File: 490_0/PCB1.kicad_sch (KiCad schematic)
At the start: 3 parts, among them J10 Conn_01x11, J3 Conn_01x08, J4 5051102291

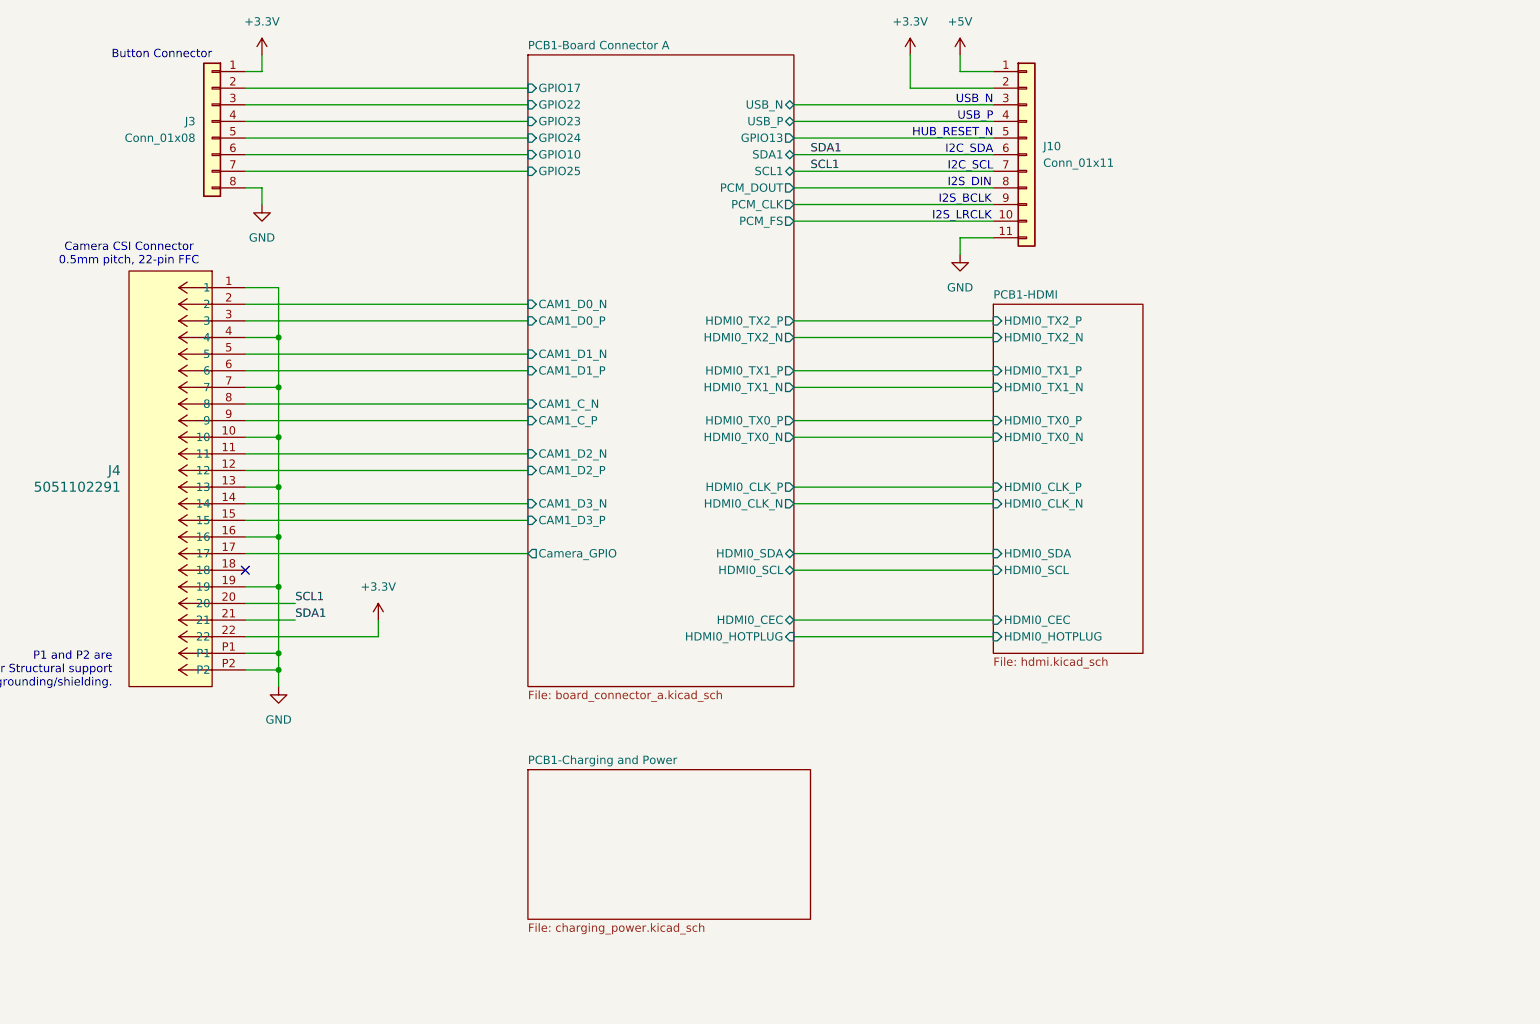
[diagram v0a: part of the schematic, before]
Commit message: Cleaned up global labels
TO DO: power chip change
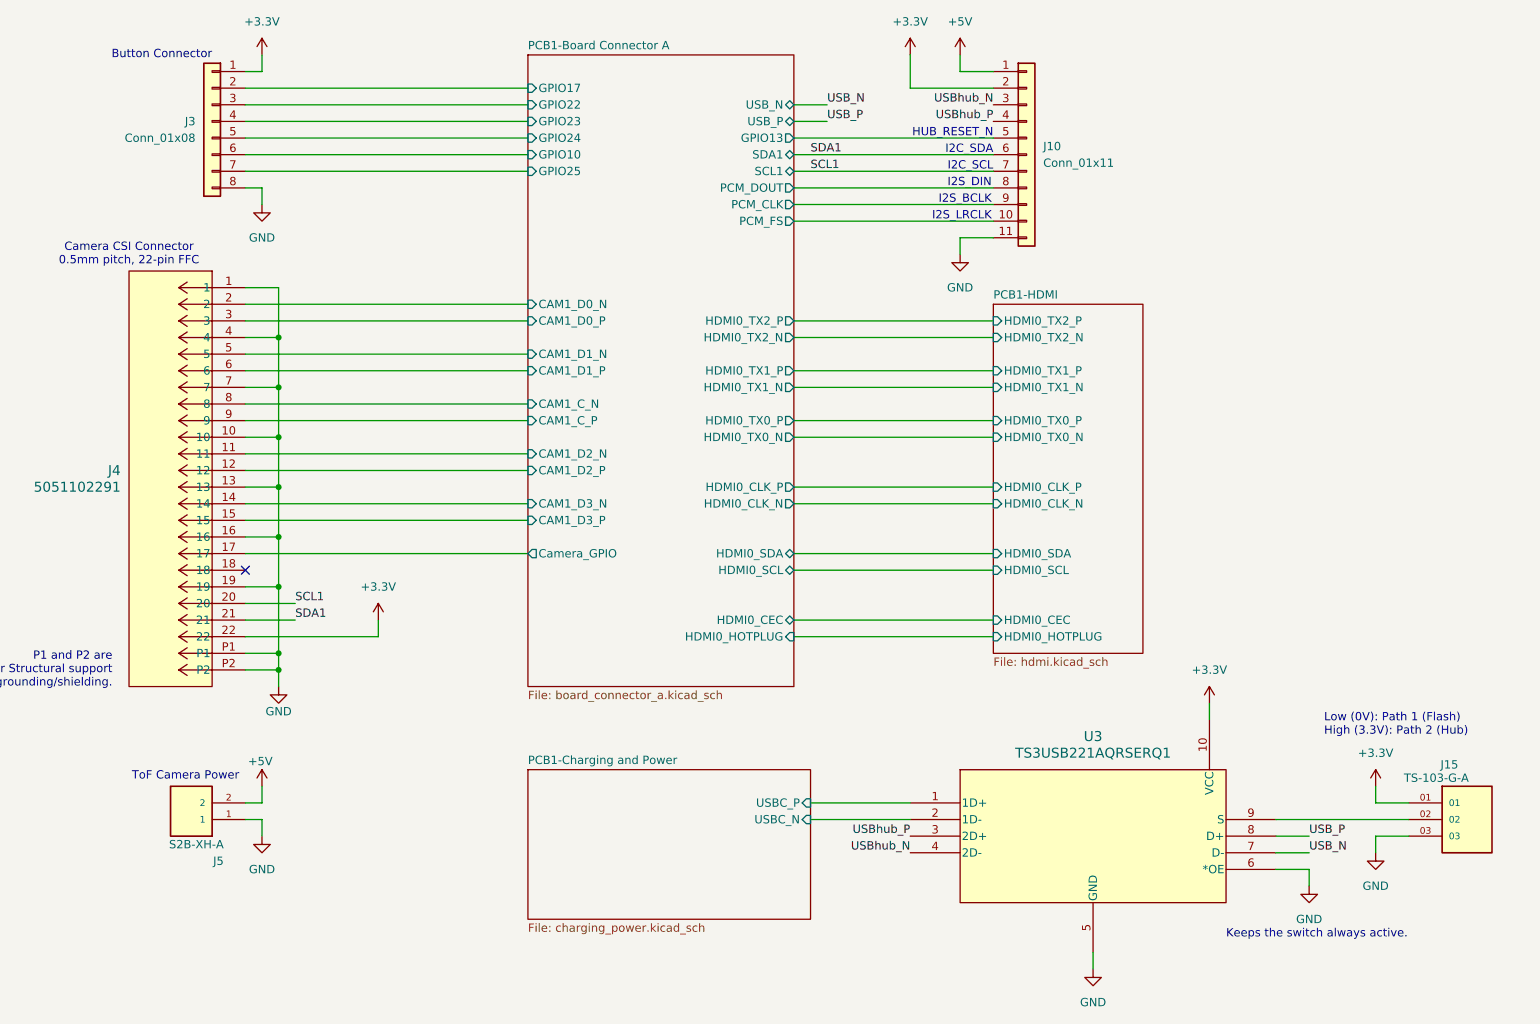
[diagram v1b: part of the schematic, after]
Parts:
- added J15: TS-103-G-A, TS-103-G-A:SAMTEC_TS-103-G-A, symbol capstone_parts:TS-103-G-A
- added J5: S2B-XH-A, S2B-XH-A:JST_S2B-XH-A, symbol capstone_parts:S2B-XH-A
- added U3: TS3USB221AQRSERQ1, RSE10, symbol capstone_parts:TS3USB221AQRSERQ1
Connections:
- net +3.3V: now also J15.01, U3.10 (VCC)
- net +5V: now also J5.2
- net GND: now also J15.03, J5.1, U3.5 (GND), U3.6 (*OE)
- net PCB1-Board Connector A/USB_N renamed USBhub_N
- net USBhub_N: now also U3.4 (2D-)
- net PCB1-Board Connector A/USB_P renamed USBhub_P
- net USBhub_P: now also U3.3 (2D+)
- new net: J15.02, U3.9 (S)
- new net PCB1-Charging and Power/USBC_N: U3.2 (1D-)
- new net PCB1-Charging and Power/USBC_P: U3.1 (1D+)
- new net USB_N: U3.7 (D-)
- new net USB_P: U3.8 (D+)
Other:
- sheet PCB1-Charging and Power ports: added USBC_N, USBC_P; removed none
- note added: "Keeps the switch always active."
- note added: "Low (0V): Path 1 (Flash) High (3.3V): Path 2 (Hub)"
- note added: "ToF Camera Power"
- note removed: "USB_N"
- note removed: "USB_P"

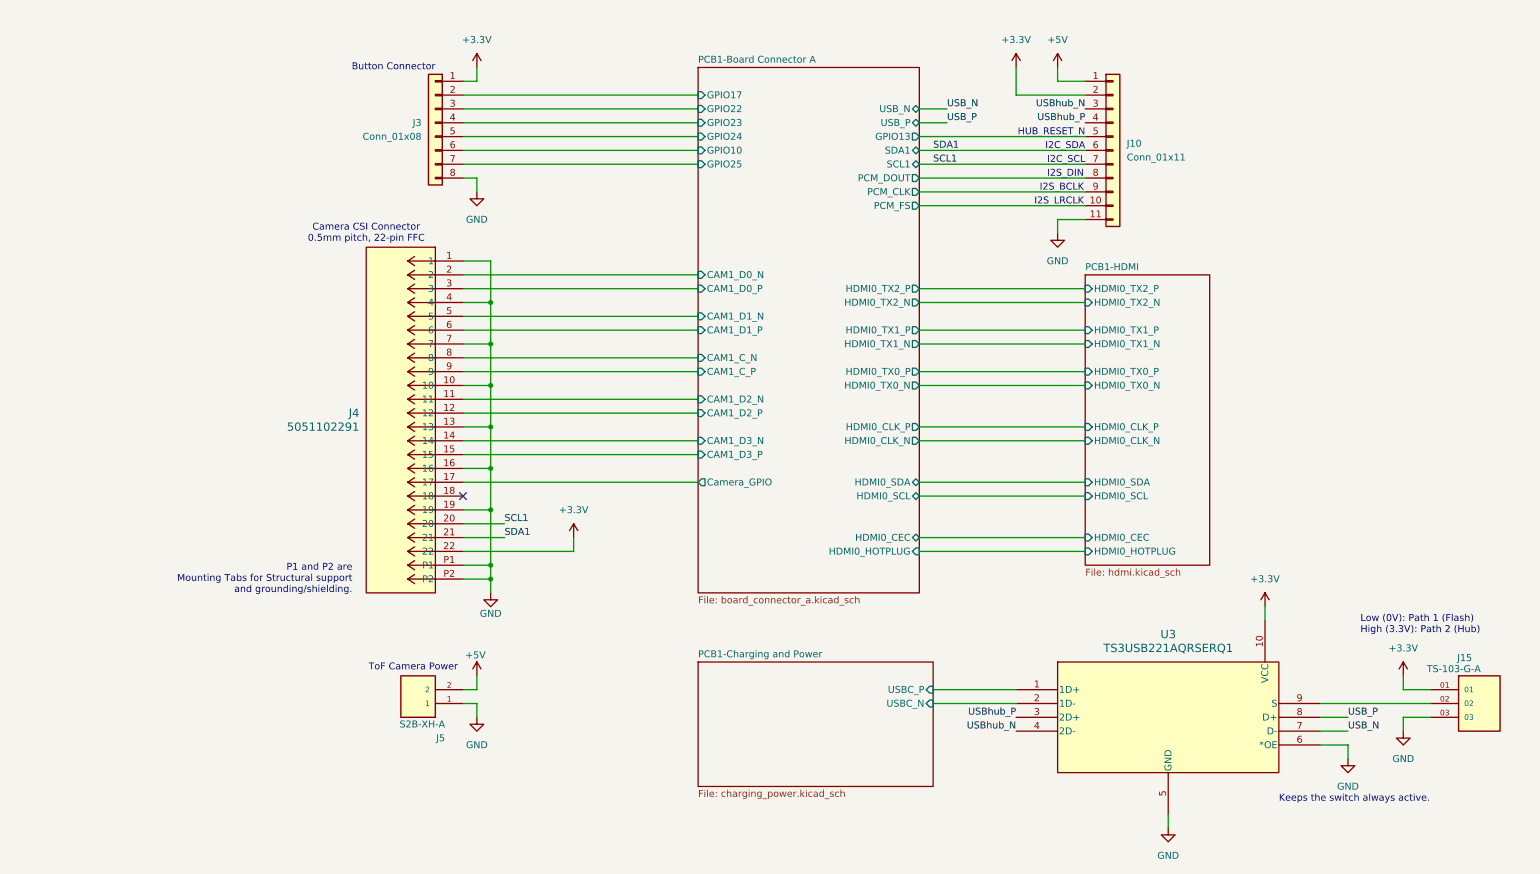
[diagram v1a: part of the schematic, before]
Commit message: Power + BOM update
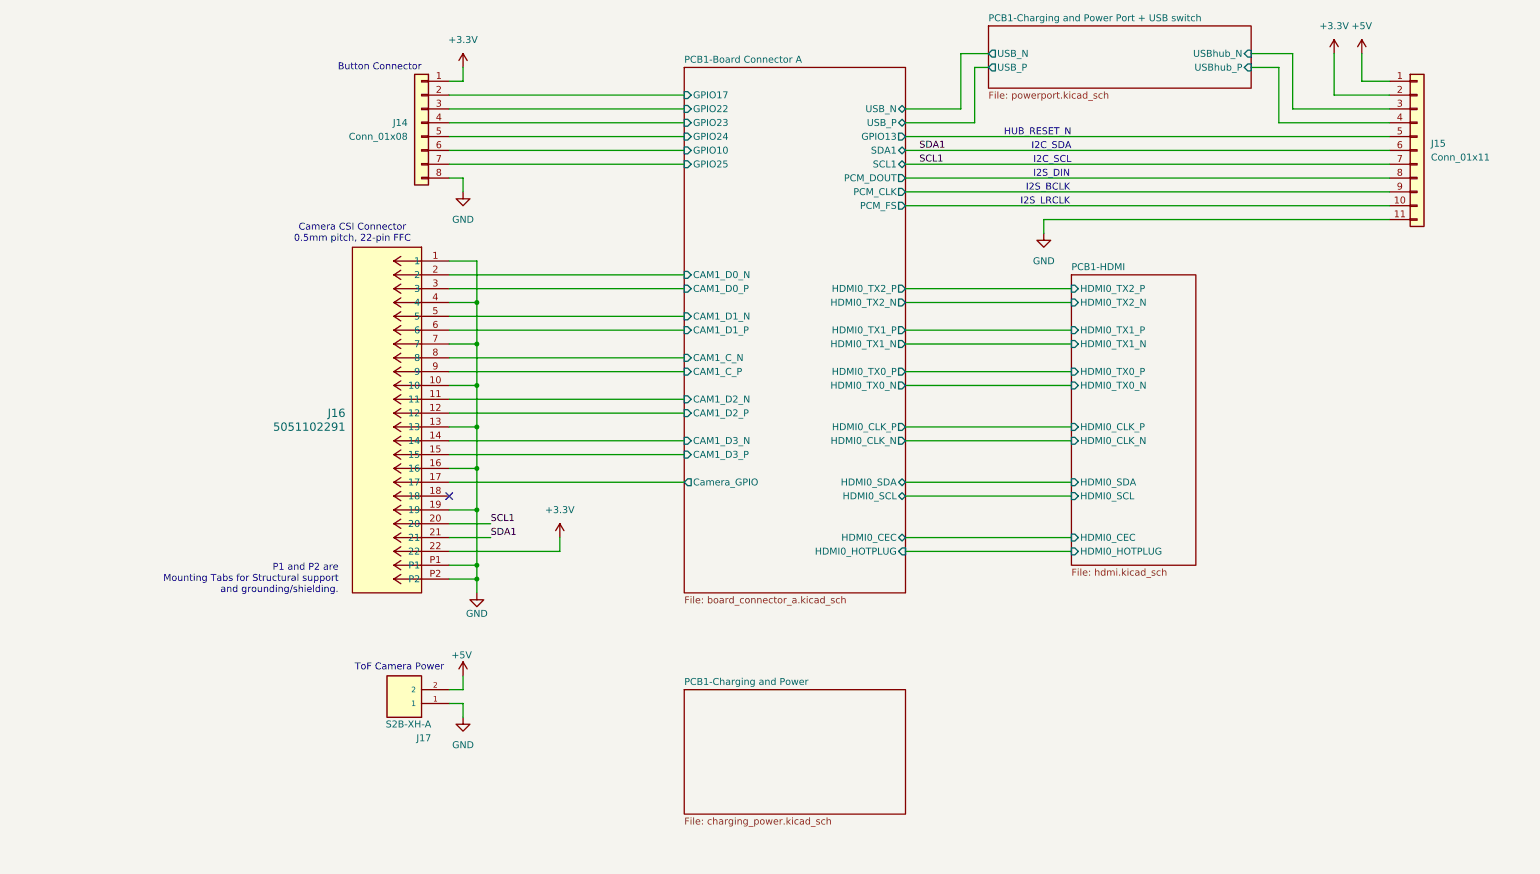
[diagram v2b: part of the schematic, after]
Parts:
- removed J15: TS-103-G-A, TS-103-G-A:SAMTEC_TS-103-G-A, symbol capstone_parts:TS-103-G-A
- removed U3: TS3USB221AQRSERQ1, RSE10, symbol capstone_parts:TS3USB221AQRSERQ1
- J14: renamed from J3; footprint 4ms_Connector:Pins_1x08_2.54mm_TH -> (none)
- J15: renamed from J10; footprint (none) -> S2B-XH-A:JST_S2B-XH-A
- J17: renamed from J5; footprint S2B-XH-A:JST_S2B-XH-A -> 4ms_Connector:Pins_1x08_2.54mm_TH
- renumbered J4 to J16
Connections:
- net USBhub_N renamed PCB1-Charging and Power Port + USB switch/USBhub_N
- net USBhub_P renamed PCB1-Charging and Power Port + USB switch/USBhub_P
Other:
- added sheet PCB1-Charging and Power Port + USB switch (powerport.kicad_sch)
- sheet PCB1-Charging and Power ports: added none; removed USBC_N, USBC_P
- note removed: "Keeps the switch always active."
- note removed: "Low (0V): Path 1 (Flash) High (3.3V): Path 2 (Hub)"
- moved on the sheet: J14, J15, J16, J17

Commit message: finished BOM
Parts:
- J14: Digikey Link (none) -> https://www.digikey.ca/en/products/detail/jst-sales-america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; Manufacturer (none) -> JST Sales America Inc.; Manufacturer Part (none) -> S8B-XH-A; Price (none) -> 0.33; Supplier (none) -> DigiKey; Supplier P/N (none) -> 455-S8B-XH-A-ND; Type (none) -> Through Hole; Unit (none) -> pcs
- J15: footprint S2B-XH-A:JST_S2B-XH-A -> (none); Digikey Link (none) -> https://www.digikey.ca/en/products/detail/jst-sales-america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; Manufacturer (none) -> JST Sales America Inc.; Manufacturer Part (none) -> S11B-XH-A; Price (none) -> 0.47; Supplier (none) -> DigiKey; Supplier P/N (none) -> 455-S11B-XH-A-ND; Type (none) -> Through Hole; Unit (none) -> pcs
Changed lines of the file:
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@@
+			)
+		)
+		(property "Voltage Raing" ""
+			(at 60.96 137.16 0)
+			(effects
+				(font
+					(size 1.27 1.27)
+				)
+				(hide yes)
+			)
+		)
+		(property "Voltage Rating" ""
+			(at 60.96 137.16 0)
+			(effects
+				(font
+					(size 1.27 1.27)
+				)
+				(hide yes)
 			)
 		)
@@
 			)
 		)
+		(property "Voltage Raing" ""
+			(at 68.58 58.42 0)
+			(effects
+				(font
+					(size 1.27 1.27)
+				)
+				(hide yes)
+			)
+		)
+		(property "Voltage Rating" ""
+			(at 68.58 58.42 0)
+			(effects
+				(font
+					(size 1.27 1.27)
+				)
+				(hide yes)
+			)
+		)
 		(pin "2"
 		)
@@
 			)
 		)
-		(property "Footprint" "S2B-XH-A:JST_S2B-XH-A"
-			(at 251.46 38.1 0)
-			(effects
-				(font
-					(size 1.27 1.27)
-				)
-				(hide yes)
-			)
-		)
-		(property "Datasheet" "~"
-			(at 251.46 38.1 0)
-			(effects
-				(font
-					(size 1.27 1.27)
-				)
-				(hide yes)
-			)
-		)
-		(property "Description" "Generic connector, single row, 01x11, script generated (kicad-library-utils/schlib/autogen/connector/)"
+		(property "Footprint" ""
+			(at 251.46 38.1 0)
+			(effects
+				(font
+					(size 1.27 1.27)
+				)
+				(hide yes)
+			)
+		)
+		(property "Datasheet" "kicad-embed://B3B-XH-A.pdf"
+			(at 251.46 38.1 0)
+			(effects
+				(font
+					(size 1.27 1.27)
+				)
+				(hide yes)
+			)
+		)
+		(property "Description" "CONN HEADER R/A 11POS 2.5MM"
+			(at 251.46 38.1 0)
+			(effects
+				(font
+					(size 1.27 1.27)
+				)
+				(hide yes)
+			)
+		)
+		(property "Digikey Link" "https://www.digikey.ca/en/products/detail/jst-sales-america-inc/S11B-XH-A/1651024"
+			(at 251.46 38.1 0)
+			(effects
+				(font
+					(size 1.27 1.27)
+				)
+				(hide yes)
+			)
+		)
+		(property "Manufacturer" "JST Sales America Inc."
+			(at 251.46 38.1 0)
+			(effects
+				(font
+					(size 1.27 1.27)
+				)
+				(hide yes)
+			)
+		)
+		(property "Manufacturer Part" "S11B-XH-A"
+			(at 251.46 38.1 0)
+			(effects
+				(font
+					(size 1.27 1.27)
+				)
+				(hide yes)
+			)
+		)
+		(property "Price" "0.47"
+			(at 251.46 38.1 0)
+			(effects
+				(font
+					(size 1.27 1.27)
+				)
+				(hide yes)
+			)
+		)
+		(property "Supplier" "DigiKey"
+			(at 251.46 38.1 0)
+			(effects
+				(font
+					(size 1.27 1.27)
+				)
+				(hide yes)
+			)
+		)
+		(property "Supplier P/N" "455-S11B-XH-A-ND"
+			(at 251.46 38.1 0)
+			(effects
+				(font
+					(size 1.27 1.27)
+				)
+				(hide yes)
+			)
+		)
+		(property "Type" "Through Hole"
+			(at 251.46 38.1 0)
+			(effects
+				(font
+					(size 1.27 1.27)
+				)
+				(hide yes)
+			)
+		)
+		(property "Unit" "pcs"
+			(at 251.46 38.1 0)
+			(effects
+				(font
+					(size 1.27 1.27)
+				)
+				(hide yes)
+			)
+		)
+		(property "Voltage Raing" ""
+			(at 251.46 38.1 0)
+			(effects
+				(font
+					(size 1.27 1.27)
+				)
+				(hide yes)
+			)
+		)
+		(property "Voltage Rating" ""
 			(at 251.46 38.1 0)
 			(effects
@@
 			)
 		)
-		(property "Datasheet" ""
+		(property "Datasheet" "kicad-embed://B3B-XH-A.pdf"
 			(at 68.58 27.94 0)
 			(effects
@@
 			)
 		)
-		(property "Description" "HEADER 1x8 MALE PINS 0.100” 180deg"
+		(property "Description" "CONN HEADER R/A 8POS 2.5MM"
 			(at 68.58 33.02 0)
 			(effects
@@
 			(at 68.58 33.02 0)
 			(effects
+				(font
+					(size 1.27 1.27)
+				)
+				(hide yes)
+			)
+		)
+		(property "Digikey Link" "https://www.digikey.ca/en/products/detail/jst-sales-america-inc/S8B-XH-A/1651023"
+			(at 68.58 33.02 0)
+			(effects
+				(font
+					(size 1.27 1.27)
+				)
+				(hide yes)
+			)
+		)
+		(property "Manufacturer" "JST Sales America Inc."
+			(at 68.58 33.02 0)
+			(effects
+				(font
+					(size 1.27 1.27)
+				)
+				(hide yes)
+			)
+		)
+		(property "Manufacturer Part" "S8B-XH-A"
+			(at 68.58 33.02 0)
+			(effects
+				(font
+					(size 1.27 1.27)
+				)
+				(hide yes)
+			)
+		)
+		(property "Price" "0.33"
+			(at 68.58 33.02 0)
+			(effects
+				(font
+					(size 1.27 1.27)
+				)
+				(hide yes)
+			)
+		)
+		(property "Supplier" "DigiKey"
+			(at 68.58 33.02 0)
+			(effects
+				(font
+					(size 1.27 1.27)
+				)
+				(hide yes)
+			)
+		)
+		(property "Supplier P/N" "455-S8B-XH-A-ND"
+			(at 68.58 33.02 0)
+			(effects
+				(font
+					(size 1.27 1.27)
+				)
+				(hide yes)
+			)
+		)
+		(property "Type" "Through Hole"
+			(at 68.58 33.02 0)
+			(effects
+				(font
+					(size 1.27 1.27)
+				)
+				(hide yes)
+			)
+		)
+		(property "Unit" "pcs"
+			(at 68.58 33.02 0)
+			(effects
+				(font
+					(size 1.27 1.27)
+				)
+				(hide yes)
+			)
+		)
+		(property "Voltage Raing" ""
+			(at 68.58 33.02 0)
+			(effects
+				(font
+					(size 1.27 1.27)
+				)
+				(hide yes)
+			)
+		)
+		(property "Voltage Rating" ""
+			(at 68.58 33.02 0)
+			(effects

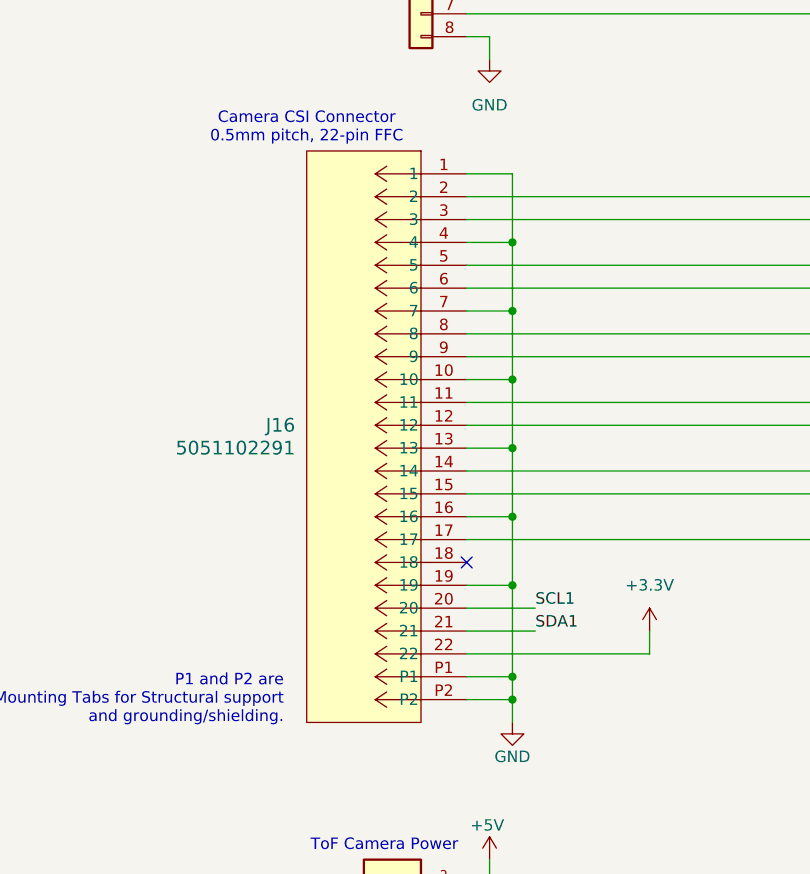
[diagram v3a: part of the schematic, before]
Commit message: Changed buck converter chip
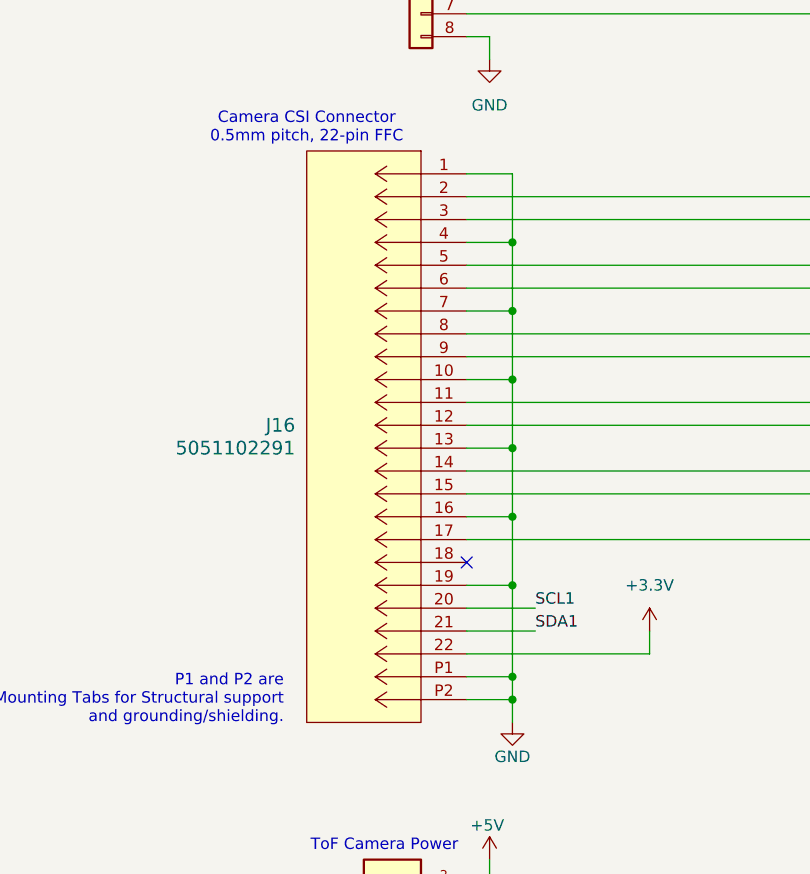
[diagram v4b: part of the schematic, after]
